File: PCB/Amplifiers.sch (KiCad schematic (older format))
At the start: 33 parts, among them U6 TL084_v, U7 LM358, U8 TL084_v

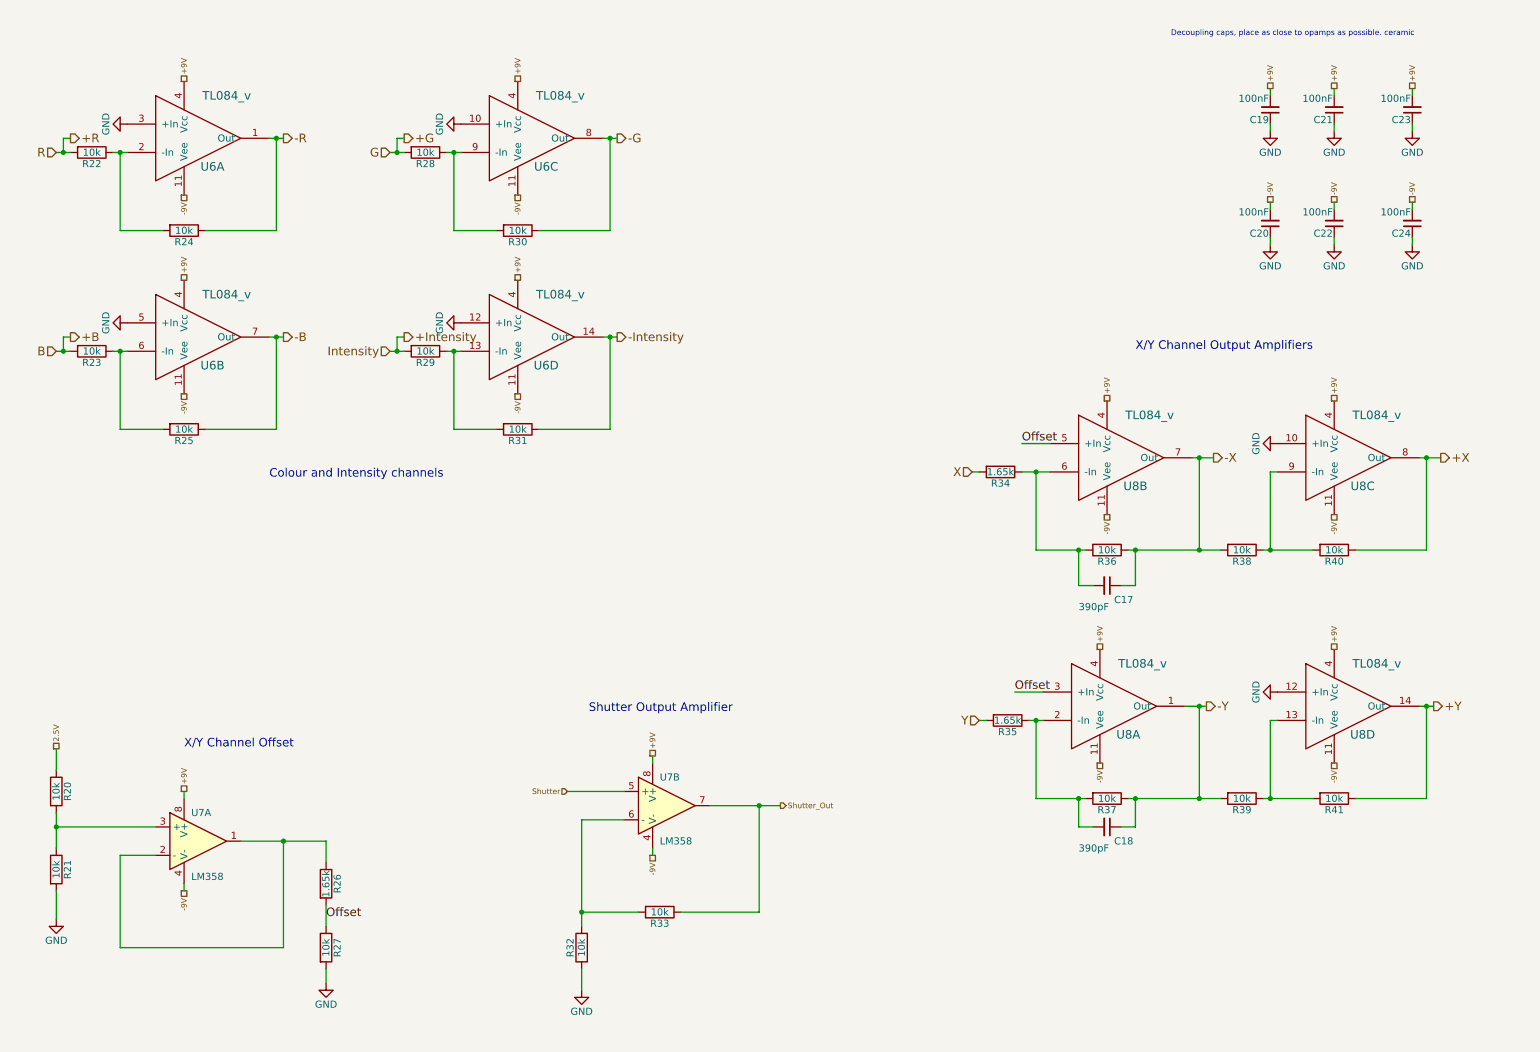
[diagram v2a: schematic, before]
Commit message: Fixed schematic errors, "small" changes to PCB
Flipped DAC, changed component values, removed 1 capacitor, moved c16
from vref to power. Developed an urge to kill kicad
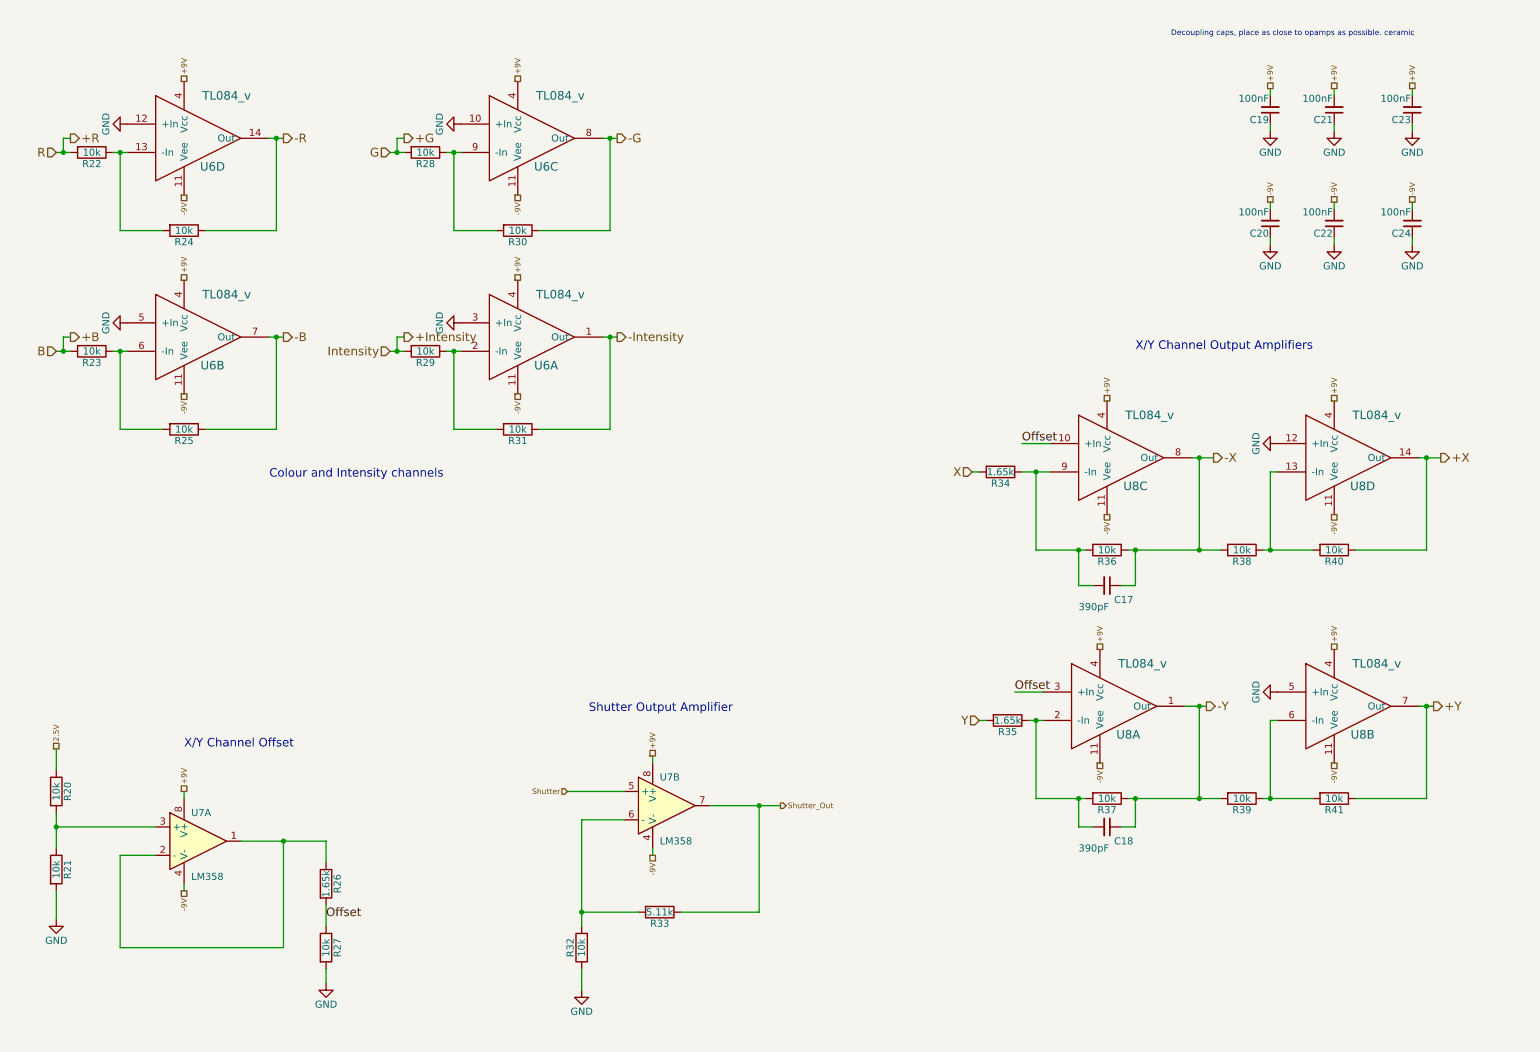
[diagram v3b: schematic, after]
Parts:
- R33: value 10k -> 5.11k
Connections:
- net +X: now also U8.14 (Out); no longer U8.8 (Out)
- net +Y: now also U8.7 (Out); no longer U8.14 (Out)
- net -Intensity: now also U6.1 (Out); no longer U6.14 (Out)
- net -R: now also U6.14 (Out); no longer U6.1 (Out)
- net -X: now also U8.8 (Out); no longer U8.7 (Out)
- net GND: now also U8.5 (+In); no longer U8.10 (+In)
- net Offset: now also U8.10 (+In); no longer U8.5 (+In)
- net at C17.2, R34.1, R36.2: now also U8.9 (-In); no longer U8.6 (-In)
- net at R39.1, R41.2: now also U8.6 (-In); no longer U8.13 (-In)
- net at R38.1, R40.2: now also U8.13 (-In); no longer U8.9 (-In)
- net at R22.1, R24.2: now also U6.13 (-In); no longer U6.2 (-In)
- net at R29.1, R31.2: now also U6.2 (-In); no longer U6.13 (-In)
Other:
- moved on the sheet: U6A, U6D, U8B, U8C, U8D
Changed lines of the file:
@@
 2.5V
 $Comp
-L GND #PWR027
+L GND #PWR026
 U 1 1 56D62C05
 P 900 6950
-F 0 "#PWR027" H 900 6700 50  0001 C CNN
+F 0 "#PWR026" H 900 6700 50  0001 C CNN
 F 1 "GND" H 900 6800 50  0000 C CNN
 F 2 "" H 900 6950 50  0000 C CNN
@@
 P 5150 6900
 F 0 "R33" V 5230 6900 50  0000 C CNN
-F 1 "10k" V 5150 6900 50  0000 C CNN
+F 1 "5.11k" V 5150 6900 50  0000 C CNN
 F 2 "Resistors_SMD:R_0805" V 5080 6900 50  0001 C CNN
 F 3 "" H 5150 6900 50  0000 C CNN
@@
 $EndComp
 $Comp
-L GND #PWR028
+L GND #PWR027
 U 1 1 56D64930
 P 4600 7450
-F 0 "#PWR028" H 4600 7200 50  0001 C CNN
+F 0 "#PWR027" H 4600 7200 50  0001 C CNN
 F 1 "GND" H 4600 7300 50  0000 C CNN
 F 2 "" H 4600 7450 50  0000 C CNN
@@
 L TL084_v U8
 U 2 1 56E9E5C2
+P 9850 5450
+F 0 "U8" H 10100 5250 60  0000 C CNN
+F 1 "TL084_v" H 10200 5750 60  0000 C CNN
+F 2 "Housings_SSOP:TSSOP-14_4.4x5mm_Pitch0.65mm" H 9850 5450 60  0001 C CNN
+F 3 "" H 9850 5450 60  0000 C CNN
+	2    9850 5450
+	1    0    0    -1
+$EndComp
+$Comp
+L TL084_v U8
+U 4 1 56E9E60F
+P 9850 3700
+F 0 "U8" H 10100 3500 60  0000 C CNN
+F 1 "TL084_v" H 10200 4000 60  0000 C CNN
+F 2 "Housings_SSOP:TSSOP-14_4.4x5mm_Pitch0.65mm" H 9850 3700 60  0001 C CNN
+F 3 "" H 9850 3700 60  0000 C CNN
+	4    9850 3700
+	1    0    0    -1
+$EndComp
+$Comp
+L TL084_v U8
+U 3 1 56E9E664
 P 8250 3700
 F 0 "U8" H 8500 3500 60  0000 C CNN
@@
 F 2 "Housings_SSOP:TSSOP-14_4.4x5mm_Pitch0.65mm" H 8250 3700 60  0001 C CNN
 F 3 "" H 8250 3700 60  0000 C CNN
-	2    8250 3700
-	1    0    0    -1
-$EndComp
-$Comp
-L TL084_v U8
-U 4 1 56E9E60F
-P 9850 5450
-F 0 "U8" H 10100 5250 60  0000 C CNN
-F 1 "TL084_v" H 10200 5750 60  0000 C CNN
-F 2 "Housings_SSOP:TSSOP-14_4.4x5mm_Pitch0.65mm" H 9850 5450 60  0001 C CNN
-F 3 "" H 9850 5450 60  0000 C CNN
-	4    9850 5450
-	1    0    0    -1
-$EndComp
-$Comp
-L TL084_v U8
-U 3 1 56E9E664
-P 9850 3700
-F 0 "U8" H 10100 3500 60  0000 C CNN
-F 1 "TL084_v" H 10200 4000 60  0000 C CNN
-F 2 "Housings_SSOP:TSSOP-14_4.4x5mm_Pitch0.65mm" H 9850 3700 60  0001 C CNN
-F 3 "" H 9850 3700 60  0000 C CNN
-	3    9850 3700
+	3    8250 3700
 	1    0    0    -1
 $EndComp
@@
 $EndComp
 $Comp
-L GND #PWR029
+L GND #PWR028
 U 1 1 56E9F32E
 P 2800 7400
-F 0 "#PWR029" H 2800 7150 50  0001 C CNN
+F 0 "#PWR028" H 2800 7150 50  0001 C CNN
 F 1 "GND" H 2800 7250 50  0000 C CNN
 F 2 "" H 2800 7400 50  0000 C CNN
@@
 +9V
 $Comp
-L GND #PWR030
+L GND #PWR029
 U 1 1 56EA231D
 P 9500 3600
-F 0 "#PWR030" H 9500 3350 50  0001 C CNN
+F 0 "#PWR029" H 9500 3350 50  0001 C CNN
 F 1 "GND" H 9500 3450 50  0000 C CNN
 F 2 "" H 9500 3600 50  0000 C CNN
@@
 +9V
 $Comp
-L GND #PWR031
+L GND #PWR030
 U 1 1 56EA45CC
 P 9500 5350
-F 0 "#PWR031" H 9500 5100 50  0001 C CNN
+F 0 "#PWR030" H 9500 5100 50  0001 C CNN
 F 1 "GND" H 9500 5200 50  0000 C CNN
 F 2 "" H 9500 5350 50  0000 C CNN
@@
 	2400 1450 2500 1450
 $Comp
-L GND #PWR032
+L GND #PWR031
 U 1 1 56EA914F
 P 1400 1350
-F 0 "#PWR032" H 1400 1100 50  0001 C CNN
+F 0 "#PWR031" H 1400 1100 50  0001 C CNN
 F 1 "GND" H 1400 1200 50  0000 C CNN
 F 2 "" H 1400 1350 50  0000 C CNN
@@
 -9V
 $Comp
-L GND #PWR033
+L GND #PWR032
 U 1 1 56EAAE4F
 P 3750 1350
-F 0 "#PWR033" H 3750 1100 50  0001 C CNN
+F 0 "#PWR032" H 3750 1100 50  0001 C CNN
 F 1 "GND" H 3750 1200 50  0000 C CNN
 F 2 "" H 3750 1350 50  0000 C CNN
@@
 $EndComp
 $Comp
-L GND #PWR034
+L GND #PWR033
 U 1 1 56EAC37C
 P 1400 2750
-F 0 "#PWR034" H 1400 2500 50  0001 C CNN
+F 0 "#PWR033" H 1400 2500 50  0001 C CNN
 F 1 "GND" H 1400 2600 50  0000 C CNN
 F 2 "" H 1400 2750 50  0000 C CNN
@@
 Connection ~ 4800 2850
 $Comp
-L GND #PWR035
+L GND #PWR034
 U 1 1 56EADE6C
 P 3750 2750
-F 0 "#PWR035" H 3750 2500 50  0001 C CNN
+F 0 "#PWR034" H 3750 2500 50  0001 C CNN
 F 1 "GND" H 3750 2600 50  0000 C CNN
 F 2 "" H 3750 2750 50  0000 C CNN
@@
 $EndComp
 $Comp
-L GND #PWR036
+L GND #PWR035
 U 1 1 56ECCA82
 P 9450 1400
-F 0 "#PWR036" H 9450 1150 50  0001 C CNN
+F 0 "#PWR035" H 9450 1150 50  0001 C CNN
 F 1 "GND" H 9450 1250 50  0000 C CNN
 F 2 "" H 9450 1400 50  0000 C CNN
@@
 $EndComp
 $Comp
-L GND #PWR037
+L GND #PWR036
 U 1 1 56ECCB03
 P 9900 1400
-F 0 "#PWR037" H 9900 1150 50  0001 C CNN
+F 0 "#PWR036" H 9900 1150 50  0001 C CNN
 F 1 "GND" H 9900 1250 50  0000 C CNN
 F 2 "" H 9900 1400 50  0000 C CNN
@@
 $EndComp
 $Comp
-L GND #PWR038
+L GND #PWR037
 U 1 1 56ECCB7D
 P 10450 1400
-F 0 "#PWR038" H 10450 1150 50  0001 C CNN
+F 0 "#PWR037" H 10450 1150 50  0001 C CNN
 F 1 "GND" H 10450 1250 50  0000 C CNN
 F 2 "" H 10450 1400 50  0000 C CNN
@@
 $EndComp
 $Comp
-L GND #PWR039
+L GND #PWR038
 U 1 1 56ECD060
 P 9450 2200
-F 0 "#PWR039" H 9450 1950 50  0001 C CNN
+F 0 "#PWR038" H 9450 1950 50  0001 C CNN
 F 1 "GND" H 9450 2050 50  0000 C CNN
 F 2 "" H 9450 2200 50  0000 C CNN
@@
 $EndComp
 $Comp
-L GND #PWR040
+L GND #PWR039
 U 1 1 56ECD066
 P 9900 2200
-F 0 "#PWR040" H 9900 1950 50  0001 C CNN
+F 0 "#PWR039" H 9900 1950 50  0001 C CNN
 F 1 "GND" H 9900 2050 50  0000 C CNN
 F 2 "" H 9900 2200 50  0000 C CNN
@@
 $EndComp
 $Comp
-L GND #PWR041
+L GND #PWR040
 U 1 1 56ECD06C
 P 10450 2200
-F 0 "#PWR041" H 10450 1950 50  0001 C CNN
+F 0 "#PWR040" H 10450 1950 50  0001 C CNN
 F 1 "GND" H 10450 2050 50  0000 C CNN
 F 2 "" H 10450 2200 50  0000 C CNN
@@
 L TL084_v U6
 U 4 1 56FAD544
-P 4100 2850
-F 0 "U6" H 4350 2650 60  0000 C CNN
-F 1 "TL084_v" H 4450 3150 60  0000 C CNN
-F 2 "Housings_SSOP:TSSOP-14_4.4x5mm_Pitch0.65mm" H 4100 2850 60  0001 C CNN
-F 3 "" H 4100 2850 60  0000 C CNN
-	4    4100 2850
+P 1750 1450
+F 0 "U6" H 2000 1250 60  0000 C CNN
+F 1 "TL084_v" H 2100 1750 60  0000 C CNN
+F 2 "Housings_SSOP:TSSOP-14_4.4x5mm_Pitch0.65mm" H 1750 1450 60  0001 C CNN
+F 3 "" H 1750 1450 60  0000 C CNN
+	4    1750 1450
 	1    0    0    -1
 $EndComp
@@
 L TL084_v U6
 U 1 1 56FAD745
-P 1750 1450
-F 0 "U6" H 2000 1250 60  0000 C CNN
-F 1 "TL084_v" H 2100 1750 60  0000 C CNN
-F 2 "Housings_SSOP:TSSOP-14_4.4x5mm_Pitch0.65mm" H 1750 1450 60  0001 C CNN
-F 3 "" H 1750 1450 60  0000 C CNN
-	1    1750 1450
-	1    0    0    -1
-$EndComp
+P 4100 2850
+F 0 "U6" H 4350 2650 60  0000 C CNN
+F 1 "TL084_v" H 4450 3150 60  0000 C CNN
+F 2 "Housings_SSOP:TSSOP-14_4.4x5mm_Pitch0.65mm" H 4100 2850 60  0001 C CNN
+F 3 "" H 4100 2850 60  0000 C CNN
+	1    4100 2850
+	1    0    0    -1
+$EndComp
